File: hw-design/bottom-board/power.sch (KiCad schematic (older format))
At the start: 18 parts, among them U1 MURATA 5V, U2 NCP1117DT50G

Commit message: Changed SODIM to Marsboard header + added liniar regulator for audio codec
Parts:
- removed C11: 100uF, Capacitors_SMD:c_elec_6.3x5.3, symbol bottom-board-rescue:CP_Small
- removed D1, D2: B130LB, Diodes_SMD:Diode-SMB_Standard, symbol bottom-board-rescue:D
- added C11: 10uF, Capacitor_SMD:C_0805_2012Metric, symbol bottom-board-rescue:C_Small-Device
- added D1, D2: MBR230, Diode_SMD:D_SOD-123F, symbol bottom-board-rescue:D_Schottky-Device
- C8: footprint Capacitors_SMD:c_elec_5x5.3 -> Capacitor_SMD:C_0805_2012Metric; symbol bottom-board-rescue:CP_Small -> bottom-board-rescue:C_Small-Device
- U2: value NCP1117DT50G -> LD1117S50TR_SOT223; footprint SMD_Packages:DPAK-2 -> Package_TO_SOT_SMD:SOT-223-3_TabPin2; symbol bottom-board-rescue:NCP1117ST50T3G -> bottom-board-rescue:LD1117S50TR_SOT223-Regulator_Linear
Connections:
- net labels added: +3V3
- wire segments 62 -> 63
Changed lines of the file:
@@
 $EndComp
 $Comp
-L bottom-board-rescue:D D1
-U 1 1 55022E7A
-P 3650 2850
-F 0 "D1" H 3650 2950 50  0000 C CNN
-F 1 "B130LB" H 3650 2750 50  0000 C CNN
-F 2 "Diodes_SMD:Diode-SMB_Standard" H 3650 2850 60  0001 C CNN
-F 3 "" H 3650 2850 60  0000 C CNN
-F 4 "B130LB-13-F" H 800 300 50  0001 C CNN "MPN"
-	1    3650 2850
-	-1   0    0    1
-$EndComp
-$Comp
-L bottom-board-rescue:D D2
-U 1 1 5502333C
-P 3650 4650
-F 0 "D2" H 3650 4750 50  0000 C CNN
-F 1 "B130LB" H 3650 4550 50  0000 C CNN
-F 2 "Diodes_SMD:Diode-SMB_Standard" H 3650 4650 60  0001 C CNN
-F 3 "" H 3650 4650 60  0000 C CNN
-F 4 "B130LB-13-F" H 800 300 50  0001 C CNN "MPN"
-	1    3650 4650
-	-1   0    0    1
-$EndComp
-$Comp
-L power:+5VA #PWR01
+L bottom-board-rescue:+5VA-power #PWR01
 U 1 1 5506CD3D
 P 8550 2650
@@
 $EndComp
 $Comp
-L power:+5V #PWR02
+L bottom-board-rescue:+5V-power #PWR02
 U 1 1 5506DB64
 P 6100 4500
@@
 $EndComp
 $Comp
-L bottom-board-rescue:CP_Small C11
-U 1 1 5506FA02
-P 8350 3050
-F 0 "C11" H 8375 3150 50  0000 L CNN
-F 1 "100uF" H 8375 2950 50  0000 L CNN
-F 2 "Capacitors_SMD:c_elec_6.3x5.3" H 8388 2900 30  0001 C CNN
-F 3 "" H 8350 3050 60  0000 C CNN
-F 4 "UWX1C101MCL1GB" H 1200 250 50  0001 C CNN "MPN"
-	1    8350 3050
-	1    0    0    -1
-$EndComp
-$Comp
-L power:GNDA #PWR03
+L bottom-board-rescue:GNDA-power #PWR03
 U 1 1 55093B7C
 P 3950 3200
+AR Path="/55093B7C" Ref="#PWR03"  Part="1"
+AR Path="/54F7244B/55093B7C" Ref="#PWR03"  Part="1"
 F 0 "#PWR03" H 3950 2950 50  0001 C CNN
 F 1 "GNDA" H 3950 3050 50  0000 C CNN
@@
 $EndComp
 $Comp
-L power:GNDA #PWR04
+L bottom-board-rescue:GNDA-power #PWR04
 U 1 1 55093C4B
 P 4300 3200
+AR Path="/55093C4B" Ref="#PWR04"  Part="1"
+AR Path="/54F7244B/55093C4B" Ref="#PWR04"  Part="1"
 F 0 "#PWR04" H 4300 2950 50  0001 C CNN
 F 1 "GNDA" H 4300 3050 50  0000 C CNN
@@
 $EndComp
 $Comp
-L power:GNDA #PWR05
+L bottom-board-rescue:GNDA-power #PWR05
 U 1 1 5509405B
 P 6850 3200
+AR Path="/5509405B" Ref="#PWR05"  Part="1"
+AR Path="/54F7244B/5509405B" Ref="#PWR05"  Part="1"
 F 0 "#PWR05" H 6850 2950 50  0001 C CNN
 F 1 "GNDA" H 6850 3050 50  0000 C CNN
@@
 $EndComp
 $Comp
-L power:GNDA #PWR06
+L bottom-board-rescue:GNDA-power #PWR06
 U 1 1 5509466E
 P 8000 3200
+AR Path="/5509466E" Ref="#PWR06"  Part="1"
+AR Path="/54F7244B/5509466E" Ref="#PWR06"  Part="1"
 F 0 "#PWR06" H 8000 2950 50  0001 C CNN
 F 1 "GNDA" H 8000 3050 50  0000 C CNN
@@
 $EndComp
 $Comp
-L power:GNDA #PWR07
+L bottom-board-rescue:GNDA-power #PWR07
 U 1 1 55094B3B
 P 8350 3200
+AR Path="/55094B3B" Ref="#PWR07"  Part="1"
+AR Path="/54F7244B/55094B3B" Ref="#PWR07"  Part="1"
 F 0 "#PWR07" H 8350 2950 50  0001 C CNN
 F 1 "GNDA" H 8350 3050 50  0000 C CNN
@@
 $EndComp
 $Comp
-L power:GNDA #PWR08
+L bottom-board-rescue:GNDA-power #PWR08
 U 1 1 550CD841
 P 7450 3250
+AR Path="/550CD841" Ref="#PWR08"  Part="1"
+AR Path="/54F7244B/550CD841" Ref="#PWR08"  Part="1"
 F 0 "#PWR08" H 7450 3000 50  0001 C CNN
 F 1 "GNDA" H 7450 3100 50  0000 C CNN
@@
 $EndComp
 $Comp
-L power:GNDA #PWR09
+L bottom-board-rescue:GNDA-power #PWR09
 U 1 1 550E1EAE
 P 5300 3200
+AR Path="/550E1EAE" Ref="#PWR09"  Part="1"
+AR Path="/54F7244B/550E1EAE" Ref="#PWR09"  Part="1"
 F 0 "#PWR09" H 5300 2950 50  0001 C CNN
 F 1 "GNDA" H 5300 3050 50  0000 C CNN
@@
 $EndComp
 $Comp
-L power:GNDA #PWR010
+L bottom-board-rescue:GNDA-power #PWR010
 U 1 1 550E1EB4
 P 5650 3200
+AR Path="/550E1EB4" Ref="#PWR010"  Part="1"
+AR Path="/54F7244B/550E1EB4" Ref="#PWR010"  Part="1"
 F 0 "#PWR010" H 5650 2950 50  0001 C CNN
 F 1 "GNDA" H 5650 3050 50  0000 C CNN
@@
 $EndComp
 $Comp
-L power:GNDD #PWR011
+L bottom-board-rescue:GNDD-power #PWR011
 U 1 1 551387EC
 P 5500 5000
@@
 $EndComp
 $Comp
-L power:GNDD #PWR012
+L bottom-board-rescue:GNDD-power #PWR012
 U 1 1 551387F2
 P 5850 5000
@@
 $EndComp
 $Comp
-L power:GNDD #PWR013
+L bottom-board-rescue:GNDD-power #PWR013
 U 1 1 55145AAF
 P 4950 5000
@@
 $EndComp
 $Comp
-L power:GNDD #PWR014
+L bottom-board-rescue:GNDD-power #PWR014
 U 1 1 55145B26
 P 4300 5000
@@
 $EndComp
 $Comp
-L power:+12VA #PWR015
+L bottom-board-rescue:+12VA-power #PWR015
 U 1 1 5515042E
 P 6000 2650
@@
 $EndComp
 $Comp
-L power:+12VA #PWR018
+L bottom-board-rescue:+12VA-power #PWR018
 U 1 1 55167A27
 P 4950 1300
@@
 $EndComp
 $Comp
-L power:PWR_FLAG #FLG019
+L bottom-board-rescue:PWR_FLAG-power #FLG019
 U 1 1 55169F5C
 P 4950 1450
@@
 $EndComp
 $Comp
-L power:GNDA #PWR020
+L bottom-board-rescue:GNDA-power #PWR020
 U 1 1 55414B11
 P 6800 1350
+AR Path="/55414B11" Ref="#PWR020"  Part="1"
+AR Path="/54F7244B/55414B11" Ref="#PWR020"  Part="1"
 F 0 "#PWR020" H 6800 1100 50  0001 C CNN
 F 1 "GNDA" H 6800 1200 50  0000 C CNN
@@
 $EndComp
 $Comp
-L power:GNDD #PWR021
+L bottom-board-rescue:GNDD-power #PWR021
 U 1 1 55414E3C
 P 7500 1350
@@
 POWER_INPUT
 $Comp
-L bottom-board-rescue:NCP1117ST50T3G U2
+L bottom-board-rescue:LD1117S50TR_SOT223-Regulator_Linear U2
 U 1 1 55712DAC
-P 7450 2900
-F 0 "U2" H 7500 2700 40  0000 C CNN
-F 1 "NCP1117DT50G" H 7450 3100 40  0000 C CNN
-F 2 "SMD_Packages:DPAK-2" H 7450 2900 60  0001 C CNN
-F 3 "" H 7450 2900 60  0000 C CNN
-F 4 "NCP1117DT50G" H 900 -1500 50  0001 C CNN "MPN"
-	1    7450 2900
-	1    0    0    -1
-$EndComp
-$Comp
-L power:+12V #PWR022
+P 7450 2850
+F 0 "U2" H 7500 2650 40  0000 C CNN
+F 1 "LD1117S50TR_SOT223" H 7450 3050 40  0000 C CNN
+F 2 "Package_TO_SOT_SMD:SOT-223-3_TabPin2" H 7450 2850 60  0001 C CNN
+F 3 "" H 7450 2850 60  0000 C CNN
+F 4 "NCP1117DT50G" H 900 -1550 50  0001 C CNN "MPN"
+	1    7450 2850
+	1    0    0    -1
+$EndComp
+$Comp
+L bottom-board-rescue:+12V-power #PWR022
 U 1 1 55F9AB1A
 P 4050 4500
@@
 $EndComp
 $Comp
-L power:+12V #PWR023
+L bottom-board-rescue:+12V-power #PWR023
 U 1 1 55F9C19E
 P 5450 1300
@@
 $EndComp
 $Comp
-L power:PWR_FLAG #FLG024
+L bottom-board-rescue:PWR_FLAG-power #FLG024
 U 1 1 55F9C1BA
 P 5450 1450
@@
 $EndComp
 $Comp
-L bottom-board-rescue:CP_Small C8
+L bottom-board-rescue:C_Small-Device C8
 U 1 1 5660158D
 P 6500 3050
 F 0 "C8" H 6550 3150 50  0000 L CNN
 F 1 "10uF" H 6300 2950 50  0000 L CNN
-F 2 "Capacitors_SMD:c_elec_5x5.3" H 6500 3050 60  0001 C CNN
+F 2 "Capacitor_SMD:C_0805_2012Metric" H 6500 3050 60  0001 C CNN
 F 3 "" H 6500 3050 60  0000 C CNN
 F 4 "UWX1E100MCL1GB" H 1400 1550 50  0001 C CNN "MPN"
@@
 $EndComp
 $Comp
-L power:GNDA #PWR025
+L bottom-board-rescue:GNDA-power #PWR025
 U 1 1 56601FC0
 P 6500 3200
+AR Path="/56601FC0" Ref="#PWR025"  Part="1"
+AR Path="/54F7244B/56601FC0" Ref="#PWR025"  Part="1"
 F 0 "#PWR025" H 6500 2950 50  0001 C CNN
 F 1 "GNDA" H 6500 3050 50  0000 C CNN
@@
 $EndComp
 $Comp
-L power:GNDD #PWR026
+L bottom-board-rescue:GNDD-power #PWR026
 U 1 1 56670B2A
 P 7500 1750
@@
 $EndComp
 $Comp
-L power:GNDA #PWR027
+L bottom-board-rescue:GNDA-power #PWR027
 U 1 1 56670B24
 P 6800 1750
+AR Path="/56670B24" Ref="#PWR027"  Part="1"
+AR Path="/54F7244B/56670B24" Ref="#PWR027"  Part="1"
 F 0 "#PWR027" H 6800 1500 50  0001 C CNN
 F 1 "GNDA" H 6800 1600 50  0000 C CNN
@@
 	6850 3150 6850 3200
 Wire Wire Line
-	7450 3150 7450 3250
-Wire Wire Line
 	8000 3150 8000 3200
 Wire Wire Line
 	8350 3150 8350 3200
-Wire Wire Line
-	7850 2850 8000 2850
 Wire Wire Line
 	8550 2850 8550 2650
@@
 	4450 1300 4450 1450
 $Comp
-L power:GNDD #PWR028
+L bottom-board-rescue:GNDD-power #PWR028
 U 1 1 55167664
 P 4450 1450
@@
 $EndComp
 $Comp
-L power:PWR_FLAG #FLG029
+L bottom-board-rescue:PWR_FLAG-power #FLG029
 U 1 1 5516947D
 P 4450 1300
@@
 	6000 2850 6500 2850
 Wire Wire Line
-	6850 2850 7050 2850
-Wire Wire Line
 	8000 2850 8350 2850
 Wire Wire Line
@@
 Wire Wire Line
 	6500 2850 6850 2850
+$Comp
+L bottom-board-rescue:+3V3-power #PWR0173
+U 1 1 5C95A933
+P 5700 1300
+F 0 "#PWR0173" H 5700 1150 50  0001 C CNN
+F 1 "+3V3" H 5715 1473 50  0000 C CNN
+F 2 "" H 5700 1300 50  0001 C CNN
+F 3 "" H 5700 1300 50  0001 C CNN
+	1    5700 1300
+	1    0    0    -1
+$EndComp
+$Comp
+L bottom-board-rescue:PWR_FLAG-power #FLG0101
+U 1 1 5C95A969
+P 5700 1450
+F 0 "#FLG0101" H 5700 1545 50  0001 C CNN
+F 1 "PWR_FLAG" H 5700 1630 50  0000 C CNN
+F 2 "" H 5700 1450 60  0000 C CNN
+F 3 "" H 5700 1450 60  0000 C CNN
+	1    5700 1450
+	-1   0    0    1
+$EndComp
+Wire Wire Line
+	5700 1300 5700 1450
+$Comp
+L bottom-board-rescue:D_Schottky-Device D1
+U 1 1 5C9A22B7
+P 3650 2850
+F 0 "D1" H 3650 2634 50  0000 C CNN
+F 1 "MBR230" H 3650 2725 50  0000 C CNN
+F 2 "Diode_SMD:D_SOD-123F" H 3650 2850 50  0001 C CNN
+F 3 "~" H 3650 2850 50  0001 C CNN
+	1    3650 2850
+	-1   0    0    1
+$EndComp
+$Comp
+L bottom-board-rescue:D_Schottky-Device D2
+U 1 1 5C9A23E3
+P 3650 4650
+F 0 "D2" H 3650 4434 50  0000 C CNN
+F 1 "MBR230" H 3650 4525 50  0000 C CNN
+F 2 "Diode_SMD:D_SOD-123F" H 3650 4650 50  0001 C CNN
+F 3 "~" H 3650 4650 50  0001 C CNN
+	1    3650 4650
+	-1   0    0    1
+$EndComp
+Wire Wire Line
+	6850 2850 7150 2850
+Wire Wire Line
+	7750 2850 8000 2850
+Wire Wire Line
+	7450 3150 7450 3250
+$Comp
+L bottom-board-rescue:C_Small-Device C11
+U 1 1 5C9A5B72
+P 8350 3050
+F 0 "C11" H 8400 3150 50  0000 L CNN
+F 1 "10uF" H 8150 2950 50  0000 L CNN
+F 2 "Capacitor_SMD:C_0805_2012Metric" H 8350 3050 60  0001 C CNN
+F 3 "" H 8350 3050 60  0000 C CNN
+F 4 "UWX1E100MCL1GB" H 3250 1550 50  0001 C CNN "MPN"
+	1    8350 3050
+	1    0    0    -1
+$EndComp
 $EndSCHEMATC

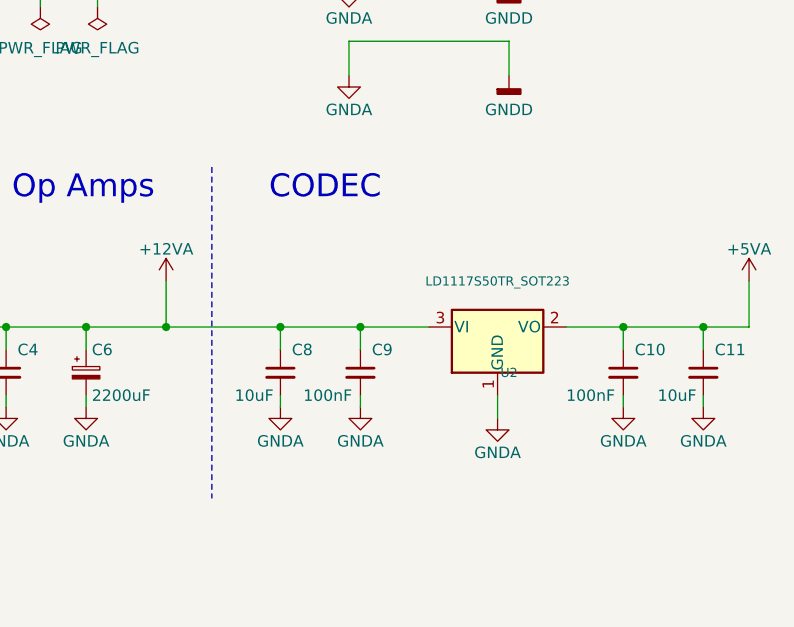
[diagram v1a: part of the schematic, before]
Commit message: changed a bottomboard to a minimal HMI testing unit
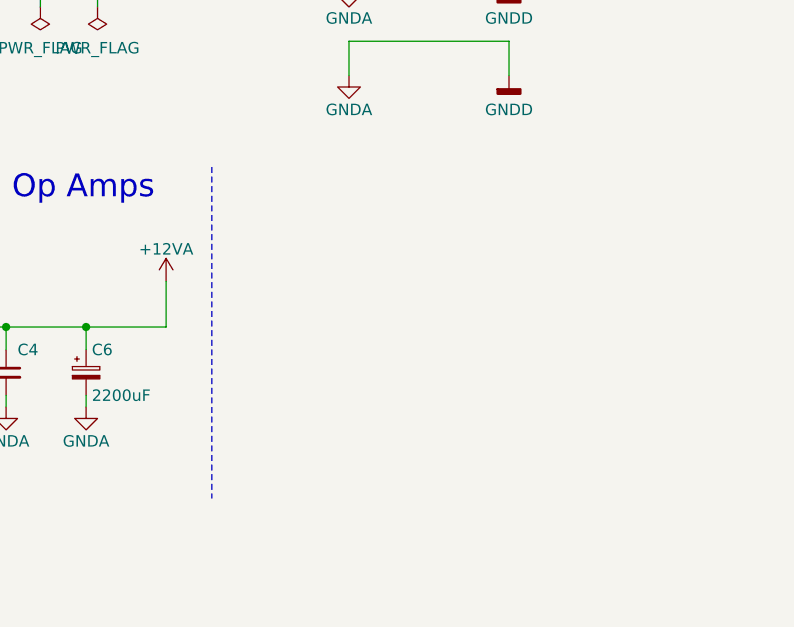
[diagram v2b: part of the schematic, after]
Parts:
- removed C10, C9: 100nF, Capacitors_SMD:C_0603, symbol bottom-board-rescue:C_Small
- removed C11, C8: 10uF, Capacitor_SMD:C_0805_2012Metric, symbol bottom-board-rescue:C_Small-Device
- removed U2: LD1117S50TR_SOT223, Package_TO_SOT_SMD:SOT-223-3_TabPin2, symbol bottom-board-rescue:LD1117S50TR_SOT223-Regulator_Linear
- C1, C4, C5: footprint Capacitors_SMD:C_0603 -> Capacitor_SMD:C_0603_1608Metric
- C2, C6: footprint Capacitors_ThroughHole:C_Radial_D10_L20_P5 -> Capacitor_THT:CP_Radial_D10.0mm_P5.00mm
- D1, D2: MPN (none) -> MBR230LSFT1G
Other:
- note removed: "CODEC"
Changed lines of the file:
@@
 EESchema Schematic File Version 4
 LIBS:bottom-board-cache
-EELAYER 26 0
+EELAYER 29 0
 EELAYER END
 $Descr A4 11693 8268
 encoding utf-8
-Sheet 2 12
-Title "MOD Duo - Bottom Board"
+Sheet 2 7
+Title "HMI testing board"
 Date ""
-Rev ""
-Comp "MOD"
-Comment1 ""
-Comment2 ""
-Comment3 ""
-Comment4 ""
+Rev "1.0"
+Comp "MOD Devices GmbH"
+Comment1 "Controller board Tester"
+Comment2 "used for the MOD Duo"
+Comment3 "or MOD Duo X controller"
+Comment4 "Compatible w/ Marsboard SoM"
 $EndDescr
 $Comp
@@
 $EndComp
 $Comp
-L bottom-board-rescue:C_Small C1
-U 1 1 54F87BFD
-P 3950 3050
-F 0 "C1" H 4000 3150 50  0000 L CNN
-F 1 "100nF" H 3700 2950 50  0000 L CNN
-F 2 "Capacitors_SMD:C_0603" H 3988 2900 30  0001 C CNN
-F 3 "" H 3950 3050 60  0000 C CNN
-F 4 "C1608X7R1E104K080AA" H 800 250 50  0001 C CNN "MPN"
-	1    3950 3050
-	1    0    0    -1
-$EndComp
-$Comp
 L bottom-board-rescue:FILTER FB1
 U 1 1 54F8818E
@@
 $EndComp
 $Comp
-L bottom-board-rescue:C_Small C9
-U 1 1 54F886BD
-P 6850 3050
-F 0 "C9" H 6900 3150 50  0000 L CNN
-F 1 "100nF" H 6600 2950 50  0000 L CNN
-F 2 "Capacitors_SMD:C_0603" H 6888 2900 30  0001 C CNN
-F 3 "" H 6850 3050 60  0000 C CNN
-F 4 "C1608X7R1E104K080AA" H 1300 250 50  0001 C CNN "MPN"
-	1    6850 3050
-	1    0    0    -1
-$EndComp
-$Comp
-L bottom-board-rescue:C_Small C10
-U 1 1 54F9954E
-P 8000 3050
-F 0 "C10" H 8050 3150 50  0000 L CNN
-F 1 "100nF" H 7750 2950 50  0000 L CNN
-F 2 "Capacitors_SMD:C_0603" H 8038 2900 30  0001 C CNN
-F 3 "" H 8000 3050 60  0000 C CNN
-F 4 "C1608X7R1E104K080AA" H 1200 250 50  0001 C CNN "MPN"
-	1    8000 3050
-	1    0    0    -1
-$EndComp
-$Comp
-L bottom-board-rescue:+5VA-power #PWR01
-U 1 1 5506CD3D
-P 8550 2650
-F 0 "#PWR01" H 8550 2500 50  0001 C CNN
-F 1 "+5VA" H 8550 2790 50  0000 C CNN
-F 2 "" H 8550 2650 60  0000 C CNN
-F 3 "" H 8550 2650 60  0000 C CNN
-	1    8550 2650
-	1    0    0    -1
-$EndComp
-$Comp
 L bottom-board-rescue:+5V-power #PWR02
 U 1 1 5506DB64
@@
 F 0 "C2" H 4325 3150 50  0000 L CNN
 F 1 "2200uF" H 4325 2950 50  0000 L CNN
-F 2 "Capacitors_ThroughHole:C_Radial_D10_L20_P5" H 4338 2900 30  0001 C CNN
-F 3 "" H 4300 3050 60  0000 C CNN
+F 2 "Capacitor_THT:CP_Radial_D10.0mm_P5.00mm" H 4338 2900 30  0001 C CNN
+F 3 "" H 4300 3050 60  0001 C CNN
 F 4 "16PX2200MEFC10X20" H 800 250 50  0001 C CNN "MPN"
 	1    4300 3050
@@
 $EndComp
 $Comp
-L bottom-board-rescue:GNDA-power #PWR05
-U 1 1 5509405B
-P 6850 3200
-AR Path="/5509405B" Ref="#PWR05"  Part="1"
-AR Path="/54F7244B/5509405B" Ref="#PWR05"  Part="1"
-F 0 "#PWR05" H 6850 2950 50  0001 C CNN
-F 1 "GNDA" H 6850 3050 50  0000 C CNN
-F 2 "" H 6850 3200 60  0000 C CNN
-F 3 "" H 6850 3200 60  0000 C CNN
-	1    6850 3200
-	1    0    0    -1
-$EndComp
-$Comp
-L bottom-board-rescue:GNDA-power #PWR06
-U 1 1 5509466E
-P 8000 3200
-AR Path="/5509466E" Ref="#PWR06"  Part="1"
-AR Path="/54F7244B/5509466E" Ref="#PWR06"  Part="1"
-F 0 "#PWR06" H 8000 2950 50  0001 C CNN
-F 1 "GNDA" H 8000 3050 50  0000 C CNN
-F 2 "" H 8000 3200 60  0000 C CNN
-F 3 "" H 8000 3200 60  0000 C CNN
-	1    8000 3200
-	1    0    0    -1
-$EndComp
-$Comp
-L bottom-board-rescue:GNDA-power #PWR07
-U 1 1 55094B3B
-P 8350 3200
-AR Path="/55094B3B" Ref="#PWR07"  Part="1"
-AR Path="/54F7244B/55094B3B" Ref="#PWR07"  Part="1"
-F 0 "#PWR07" H 8350 2950 50  0001 C CNN
-F 1 "GNDA" H 8350 3050 50  0000 C CNN
-F 2 "" H 8350 3200 60  0000 C CNN
-F 3 "" H 8350 3200 60  0000 C CNN
-	1    8350 3200
-	1    0    0    -1
-$EndComp
-$Comp
-L bottom-board-rescue:GNDA-power #PWR08
-U 1 1 550CD841
-P 7450 3250
-AR Path="/550CD841" Ref="#PWR08"  Part="1"
-AR Path="/54F7244B/550CD841" Ref="#PWR08"  Part="1"
-F 0 "#PWR08" H 7450 3000 50  0001 C CNN
-F 1 "GNDA" H 7450 3100 50  0000 C CNN
-F 2 "" H 7450 3250 60  0000 C CNN
-F 3 "" H 7450 3250 60  0000 C CNN
-	1    7450 3250
-	1    0    0    -1
-$EndComp
-$Comp
-L bottom-board-rescue:C_Small C4
-U 1 1 550E1E9E
-P 5300 3050
-F 0 "C4" H 5350 3150 50  0000 L CNN
-F 1 "100nF" H 5050 2950 50  0000 L CNN
-F 2 "Capacitors_SMD:C_0603" H 5338 2900 30  0001 C CNN
-F 3 "" H 5300 3050 60  0000 C CNN
-F 4 "C1608X7R1E104K080AA" H 800 250 50  0001 C CNN "MPN"
-	1    5300 3050
-	1    0    0    -1
-$EndComp
-$Comp
-L bottom-board-rescue:CP_Small C6
-U 1 1 550E1EA8
-P 5650 3050
-F 0 "C6" H 5675 3150 50  0000 L CNN
-F 1 "2200uF" H 5675 2950 50  0000 L CNN
-F 2 "Capacitors_ThroughHole:C_Radial_D10_L20_P5" H 5688 2900 30  0001 C CNN
-F 3 "" H 5650 3050 60  0000 C CNN
-F 4 "16PX2200MEFC10X20" H 800 250 50  0001 C CNN "MPN"
-	1    5650 3050
-	1    0    0    -1
-$EndComp
-$Comp
 L bottom-board-rescue:GNDA-power #PWR09
 U 1 1 550E1EAE
@@
 F 0 "C5" H 5550 4950 50  0000 L CNN
 F 1 "100nF" H 5250 4750 50  0000 L CNN
-F 2 "Capacitors_SMD:C_0603" H 5538 4700 30  0001 C CNN
-F 3 "" H 5500 4850 60  0000 C CNN
+F 2 "Capacitor_SMD:C_0603_1608Metric" H 5538 4700 30  0001 C CNN
+F 3 "" H 5500 4850 60  0001 C CNN
 F 4 "C1608X7R1E104K080AA" H -1600 250 50  0001 C CNN "MPN"
 	1    5500 4850
@@
 POWER_INPUT
 $Comp
-L bottom-board-rescue:LD1117S50TR_SOT223-Regulator_Linear U2
-U 1 1 55712DAC
-P 7450 2850
-F 0 "U2" H 7500 2650 40  0000 C CNN
-F 1 "LD1117S50TR_SOT223" H 7450 3050 40  0000 C CNN
-F 2 "Package_TO_SOT_SMD:SOT-223-3_TabPin2" H 7450 2850 60  0001 C CNN
-F 3 "" H 7450 2850 60  0000 C CNN
-F 4 "NCP1117DT50G" H 900 -1550 50  0001 C CNN "MPN"
-	1    7450 2850
-	1    0    0    -1
-$EndComp
-$Comp
 L bottom-board-rescue:+12V-power #PWR022
 U 1 1 55F9AB1A
@@
 	1    0    0    -1
 $EndComp
-$Comp
-L bottom-board-rescue:C_Small-Device C8
-U 1 1 5660158D
-P 6500 3050
-F 0 "C8" H 6550 3150 50  0000 L CNN
-F 1 "10uF" H 6300 2950 50  0000 L CNN
-F 2 "Capacitor_SMD:C_0805_2012Metric" H 6500 3050 60  0001 C CNN
-F 3 "" H 6500 3050 60  0000 C CNN
-F 4 "UWX1E100MCL1GB" H 1400 1550 50  0001 C CNN "MPN"
-	1    6500 3050
-	1    0    0    -1
-$EndComp
-$Comp
-L bottom-board-rescue:GNDA-power #PWR025
-U 1 1 56601FC0
-P 6500 3200
-AR Path="/56601FC0" Ref="#PWR025"  Part="1"
-AR Path="/54F7244B/56601FC0" Ref="#PWR025"  Part="1"
-F 0 "#PWR025" H 6500 2950 50  0001 C CNN
-F 1 "GNDA" H 6500 3050 50  0000 C CNN
-F 2 "" H 6500 3200 60  0000 C CNN
-F 3 "" H 6500 3200 60  0000 C CNN
-	1    6500 3200
-	1    0    0    -1
-$EndComp
 Text Notes 5950 2300 2    100  ~ 0
 Op Amps
-Text Notes 6450 2300 0    100  ~ 0
-CODEC
 Text Notes 5200 4200 2    100  ~ 0
 Digital
@@
 	6000 2650 6000 2850
 Wire Wire Line
-	6850 2850 6850 2950
-Wire Wire Line
-	6850 3150 6850 3200
-Wire Wire Line
-	8000 3150 8000 3200
-Wire Wire Line
-	8350 3150 8350 3200
-Wire Wire Line
-	8550 2850 8550 2650
-Wire Wire Line
-	8000 2850 8000 2950
-Wire Wire Line
-	8350 2950 8350 2850
-Wire Wire Line
 	4300 4950 4300 5000
 Wire Wire Line
@@
 Connection ~ 3950 2850
 Connection ~ 4300 2850
-Connection ~ 6000 2850
-Connection ~ 6850 2850
-Connection ~ 8000 2850
-Connection ~ 8350 2850
 Connection ~ 4300 4650
 Connection ~ 5300 2850
@@
 Wire Wire Line
 	5150 2850 5300 2850
-Wire Wire Line
-	6500 2950 6500 2850
-Connection ~ 6500 2850
-Wire Wire Line
-	6500 3150 6500 3200
 Wire Wire Line
 	7500 1600 7500 1750
@@
 	4300 2850 4450 2850
 Wire Wire Line
-	6000 2850 6500 2850
-Wire Wire Line
-	8000 2850 8350 2850
-Wire Wire Line
-	8350 2850 8550 2850
-Wire Wire Line
 	4300 4650 4550 4650
 Wire Wire Line
@@
 Wire Wire Line
 	4050 4650 4300 4650
-Wire Wire Line
-	6500 2850 6850 2850
 $Comp
 L bottom-board-rescue:+3V3-power #PWR0173
@@
 F 1 "MBR230" H 3650 2725 50  0000 C CNN
 F 2 "Diode_SMD:D_SOD-123F" H 3650 2850 50  0001 C CNN
-F 3 "~" H 3650 2850 50  0001 C CNN
+F 3 "" H 3650 2850 50  0001 C CNN
+F 4 "MBR230LSFT1G" H 3650 2850 50  0001 C CNN "MPN"
 	1    3650 2850
 	-1   0    0    1
@@
 F 1 "MBR230" H 3650 4525 50  0000 C CNN
 F 2 "Diode_SMD:D_SOD-123F" H 3650 4650 50  0001 C CNN
-F 3 "~" H 3650 4650 50  0001 C CNN
+F 3 "" H 3650 4650 50  0001 C CNN
+F 4 "MBR230LSFT1G" H 3650 4650 50  0001 C CNN "MPN"
 	1    3650 4650
 	-1   0    0    1
 $EndComp
-Wire Wire Line
-	6850 2850 7150 2850
-Wire Wire Line
-	7750 2850 8000 2850
-Wire Wire Line
-	7450 3150 7450 3250
-$Comp
-L bottom-board-rescue:C_Small-Device C11
-U 1 1 5C9A5B72
-P 8350 3050
-F 0 "C11" H 8400 3150 50  0000 L CNN
-F 1 "10uF" H 8150 2950 50  0000 L CNN
-F 2 "Capacitor_SMD:C_0805_2012Metric" H 8350 3050 60  0001 C CNN
-F 3 "" H 8350 3050 60  0000 C CNN
-F 4 "UWX1E100MCL1GB" H 3250 1550 50  0001 C CNN "MPN"
-	1    8350 3050
-	1    0    0    -1
-$EndComp
+$Comp
+L bottom-board-rescue:C_Small C4
+U 1 1 550E1E9E
+P 5300 3050
+F 0 "C4" H 5350 3150 50  0000 L CNN
+F 1 "100nF" H 5050 2950 50  0000 L CNN
+F 2 "Capacitor_SMD:C_0603_1608Metric" H 5338 2900 30  0001 C CNN
+F 3 "" H 5300 3050 60  0001 C CNN
+F 4 "C1608X7R1E104K080AA" H 800 250 50  0001 C CNN "MPN"
+	1    5300 3050
+	1    0    0    -1
+$EndComp
+$Comp
+L bottom-board-rescue:C_Small C1
+U 1 1 54F87BFD
+P 3950 3050
+F 0 "C1" H 4000 3150 50  0000 L CNN
+F 1 "100nF" H 3700 2950 50  0000 L CNN
+F 2 "Capacitor_SMD:C_0603_1608Metric" H 3988 2900 30  0001 C CNN
+F 3 "" H 3900 3150 60  0001 C CNN
+F 4 "C1608X7R1E104K080AA" H 800 250 50  0001 C CNN "MPN"
+	1    3950 3050
+	1    0    0    -1
+$EndComp
+$Comp
+L bottom-board-rescue:CP_Small C6
+U 1 1 550E1EA8
+P 5650 3050
+F 0 "C6" H 5675 3150 50  0000 L CNN
+F 1 "2200uF" H 5675 2950 50  0000 L CNN
+F 2 "Capacitor_THT:CP_Radial_D10.0mm_P5.00mm" H 5688 2900 30  0001 C CNN
+F 3 "" H 5650 3050 60  0001 C CNN
+F 4 "16PX2200MEFC10X20" H 800 250 50  0001 C CNN "MPN"
+	1    5650 3050
+	1    0    0    -1
+$EndComp
